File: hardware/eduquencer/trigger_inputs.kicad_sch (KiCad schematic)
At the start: 15 parts, among them Q1 MMBT3904

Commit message: Hardware: add test points, tiny cleanup
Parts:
- J?: value Jack_Trigger_In_B -> Reset In
- J?: value Jack_Trigger_In_A -> Clock In
- Q1, Q?: LCSC C20526 -> (none); LCSC Part # C20526 -> (none)
- R14, R15, R? (x2): LCSC C25803 -> (none); LCSC Part # C25803 -> (none)
- R16, R?: LCSC C4216 -> (none); LCSC Part # C4216 -> (none)
- R17, R?: LCSC C25804 -> (none); LCSC Part # C25804 -> (none)
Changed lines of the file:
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@@
       (effects (font (size 1.27 1.27)) (justify left) hide)
     )
-    (property "LCSC Part #" "C20526" (id 4) (at 132.08 60.96 0)
-      (effects (font (size 1.27 1.27)) hide)
-    )
-    (property "LCSC" "C20526" (id 5) (at 132.08 60.96 0)
-      (effects (font (size 1.27 1.27)) hide)
-    )
     (pin "1")
     (pin "2")
@@
       (effects (font (size 1.27 1.27)) hide)
     )
-    (property "LCSC Part #" "C25804" (id 4) (at 134.62 46.99 0)
-      (effects (font (size 1.27 1.27)) hide)
-    )
-    (property "LCSC" "C25804" (id 5) (at 134.62 46.99 0)
-      (effects (font (size 1.27 1.27)) hide)
-    )
     (pin "1")
     (pin "2")
@@
     )
     (property "Datasheet" "~" (id 3) (at 69.85 43.18 0)
-      (effects (font (size 1.27 1.27)) hide)
-    )
-    (property "LCSC Part #" "C25803" (id 4) (at 69.85 43.18 0)
-      (effects (font (size 1.27 1.27)) hide)
-    )
-    (property "LCSC" "C25803" (id 5) (at 69.85 43.18 0)
       (effects (font (size 1.27 1.27)) hide)
     )
@@
       (effects (font (size 1.27 1.27)) hide)
     )
-    (property "LCSC Part #" "C25803" (id 4) (at 96.52 60.96 0)
-      (effects (font (size 1.27 1.27)) hide)
-    )
-    (property "LCSC" "C25803" (id 5) (at 96.52 60.96 0)
-      (effects (font (size 1.27 1.27)) hide)
-    )
     (pin "1")
     (pin "2")
@@
     )
     (property "Datasheet" "~" (id 3) (at 118.11 74.93 0)
-      (effects (font (size 1.27 1.27)) hide)
-    )
-    (property "LCSC Part #" "C4216" (id 4) (at 118.11 74.93 0)
-      (effects (font (size 1.27 1.27)) hide)
-    )
-    (property "LCSC" "C4216" (id 5) (at 118.11 74.93 0)
       (effects (font (size 1.27 1.27)) hide)
     )
@@
   (symbol (lib_id "power:GND") (at 83.82 162.56 0) (unit 1)
     (in_bom yes) (on_board yes)
-    (property "Reference" "#PWR?" (id 0) (at 83.82 168.91 0)
+    (property "Reference" "#PWR0163" (id 0) (at 83.82 168.91 0)
       (effects (font (size 1.27 1.27)) hide)
     )
@@
   (symbol (lib_id "power:GND") (at 134.62 162.56 0) (unit 1)
     (in_bom yes) (on_board yes)
-    (property "Reference" "#PWR?" (id 0) (at 134.62 168.91 0)
+    (property "Reference" "#PWR0161" (id 0) (at 134.62 168.91 0)
       (effects (font (size 1.27 1.27)) hide)
     )
@@
   (symbol (lib_id "power:GND") (at 118.11 162.56 0) (unit 1)
     (in_bom yes) (on_board yes)
-    (property "Reference" "#PWR?" (id 0) (at 118.11 168.91 0)
+    (property "Reference" "#PWR0160" (id 0) (at 118.11 168.91 0)
       (effects (font (size 1.27 1.27)) hide)
     )
@@
       (effects (font (size 1.27 1.27)) hide)
     )
-    (property "LCSC Part #" "C25803" (id 4) (at 96.52 140.97 0)
-      (effects (font (size 1.27 1.27)) hide)
-    )
-    (property "LCSC" "C25803" (id 5) (at 96.52 140.97 0)
-      (effects (font (size 1.27 1.27)) hide)
-    )
     (pin "1")
     (pin "2")
@@
       (effects (font (size 1.27 1.27)) (justify right))
     )
-    (property "Value" "Jack_Trigger_In_B" (id 1) (at 50.8 141.6049 0)
+    (property "Value" "Reset In" (id 1) (at 50.8 141.6049 0)
       (effects (font (size 1.27 1.27)) (justify right))
     )
@@
       (effects (font (size 1.27 1.27)) (justify right))
     )
-    (property "Value" "Jack_Trigger_In_A" (id 1) (at 50.8 61.5949 0)
+    (property "Value" "Clock In" (id 1) (at 50.8 61.5949 0)
       (effects (font (size 1.27 1.27)) (justify right))
     )
@@
       (effects (font (size 1.27 1.27)) hide)
     )
-    (property "LCSC Part #" "C25803" (id 4) (at 69.85 123.19 0)
-      (effects (font (size 1.27 1.27)) hide)
-    )
-    (property "LCSC" "C25803" (id 5) (at 69.85 123.19 0)
-      (effects (font (size 1.27 1.27)) hide)
-    )
     (pin "1")
     (pin "2")
@@
   (symbol (lib_id "power:GND") (at 64.77 148.59 0) (unit 1)
     (in_bom yes) (on_board yes)
-    (property "Reference" "#PWR?" (id 0) (at 64.77 154.94 0)
+    (property "Reference" "#PWR0164" (id 0) (at 64.77 154.94 0)
       (effects (font (size 1.27 1.27)) hide)
     )
@@
       (effects (font (size 1.27 1.27)) (justify left) hide)
     )
-    (property "LCSC Part #" "C20526" (id 4) (at 132.08 140.97 0)
-      (effects (font (size 1.27 1.27)) hide)
-    )
-    (property "LCSC" "C20526" (id 5) (at 132.08 140.97 0)
-      (effects (font (size 1.27 1.27)) hide)
-    )
     (pin "1")
     (pin "2")
@@
   (symbol (lib_id "power:GND") (at 220.98 57.15 0) (unit 1)
     (in_bom yes) (on_board yes)
-    (property "Reference" "#PWR?" (id 0) (at 220.98 63.5 0)
+    (property "Reference" "#PWR0165" (id 0) (at 220.98 63.5 0)
       (effects (font (size 1.27 1.27)) hide)
     )
@@
     )
     (property "Datasheet" "~" (id 3) (at 134.62 127 0)
-      (effects (font (size 1.27 1.27)) hide)
-    )
-    (property "LCSC Part #" "C25804" (id 4) (at 134.62 127 0)
-      (effects (font (size 1.27 1.27)) hide)
-    )
-    (property "LCSC" "C25804" (id 5) (at 134.62 127 0)
       (effects (font (size 1.27 1.27)) hide)
     )
@@
       (effects (font (size 1.27 1.27)) hide)
     )
-    (property "LCSC Part #" "C4216" (id 4) (at 118.11 154.94 0)
-      (effects (font (size 1.27 1.27)) hide)
-    )
-    (property "LCSC" "C4216" (id 5) (at 118.11 154.94 0)
-      (effects (font (size 1.27 1.27)) hide)
-    )
     (pin "1")
     (pin "2")
@@
   (symbol (lib_id "power:+3.3V") (at 134.62 120.65 0) (unit 1)
     (in_bom yes) (on_board yes)
-    (property "Reference" "#PWR?" (id 0) (at 134.62 124.46 0)
+    (property "Reference" "#PWR0162" (id 0) (at 134.62 124.46 0)
       (effects (font (size 1.27 1.27)) hide)
     )
@@
   (symbol (lib_id "power:+3.3V") (at 220.98 41.91 0) (unit 1)
     (in_bom yes) (on_board yes)
-    (property "Reference" "#PWR?" (id 0) (at 220.98 45.72 0)
-      (effects (font (size 1.27 1.27)) hide)
-    )
+    (property "Reference" "#PWR0166" (id 0) (at 220.98 45.72 0)
+      (effects (font (size 1.27 1.27)) hide)
+    )

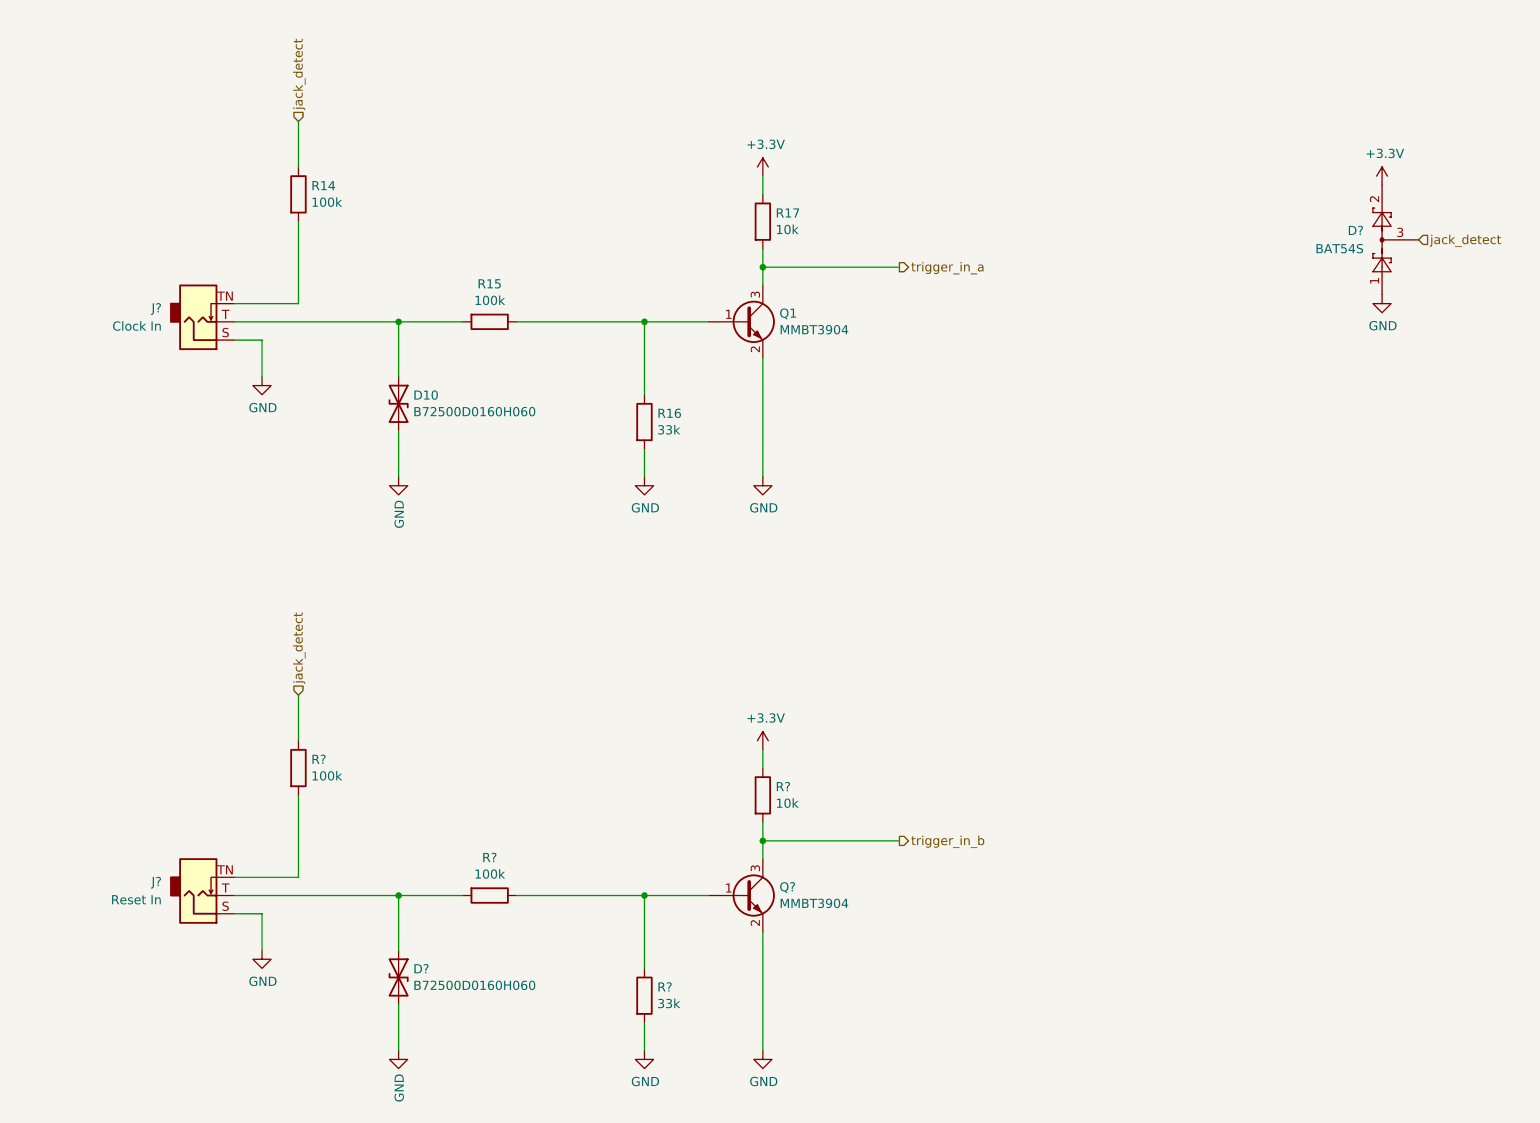
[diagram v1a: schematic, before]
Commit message: Hardware: update models, annotate, fix ERC issues
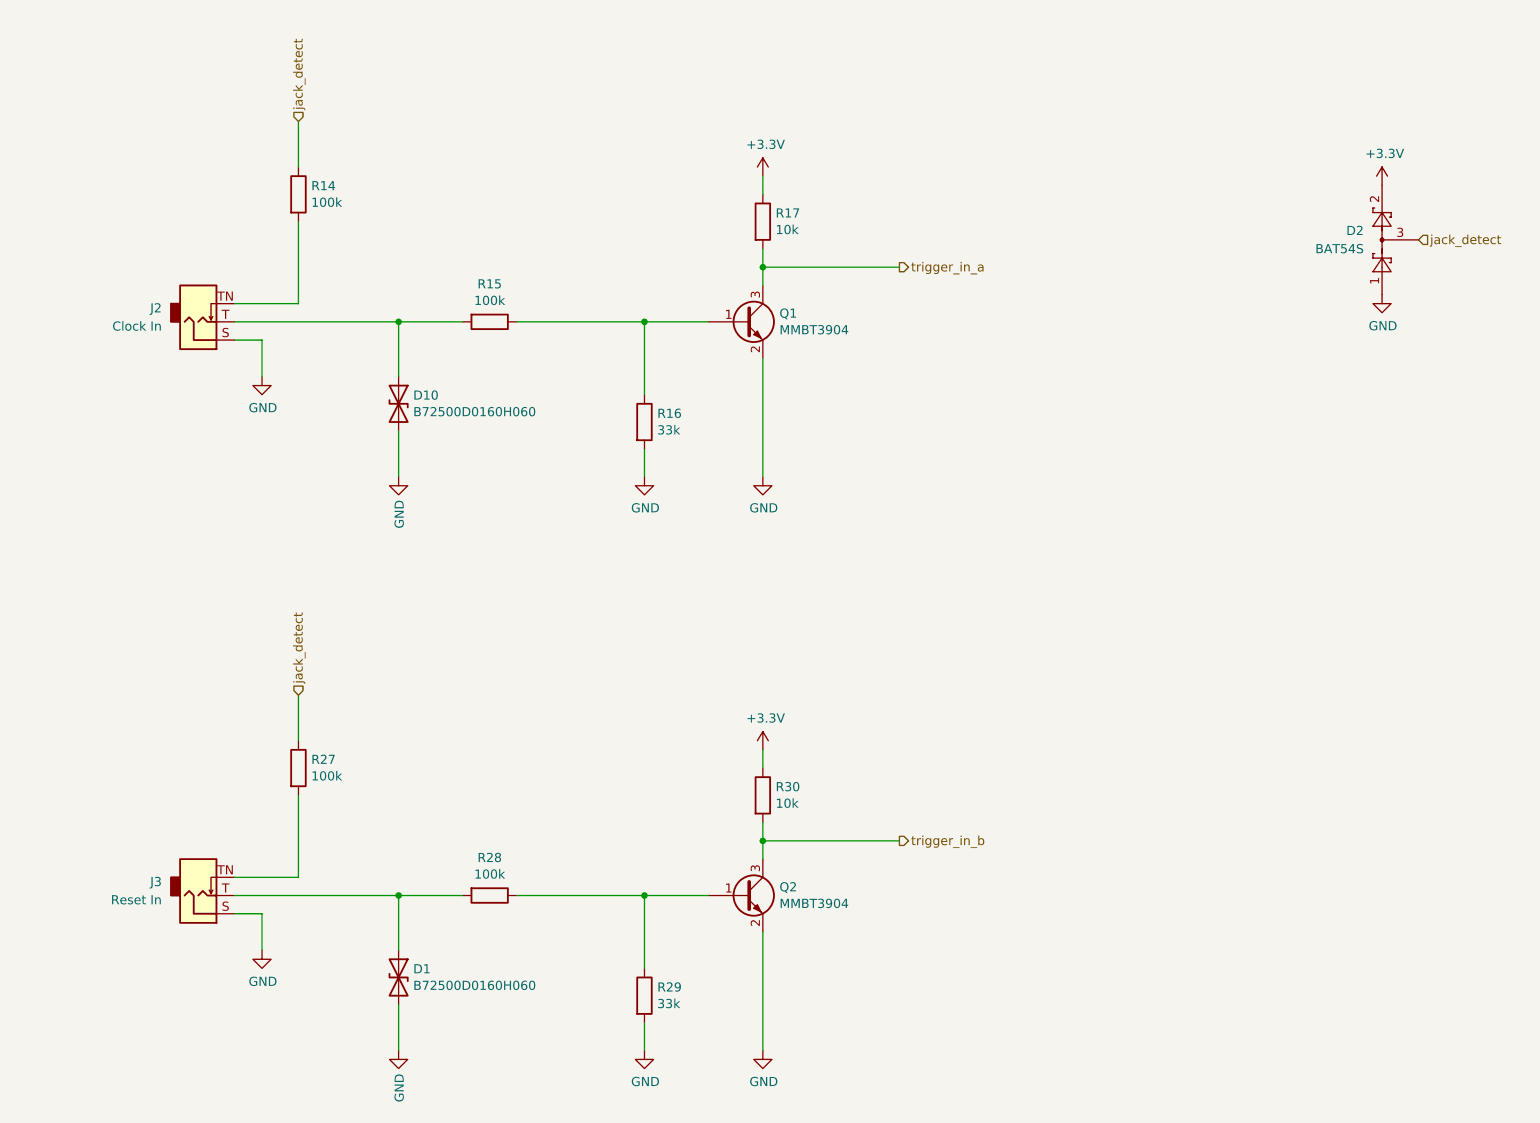
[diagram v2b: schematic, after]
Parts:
- gave numbers to parts that had none: 9
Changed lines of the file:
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@@
   (symbol (lib_id "Device:R") (at 96.52 140.97 270) (unit 1)
     (in_bom yes) (on_board yes)
-    (property "Reference" "R?" (id 0) (at 96.52 135.7122 90))
+    (property "Reference" "R28" (id 0) (at 96.52 135.7122 90))
     (property "Value" "100k" (id 1) (at 96.52 138.0236 90))
     (property "Footprint" "Resistor_SMD:R_0603_1608Metric" (id 2) (at 96.52 139.192 90)
@@
   (symbol (lib_id "Connector:AudioJack2_SwitchT") (at 55.88 140.97 0) (mirror x) (unit 1)
     (in_bom yes) (on_board yes) (fields_autoplaced)
-    (property "Reference" "J?" (id 0) (at 50.8 139.0649 0)
+    (property "Reference" "J3" (id 0) (at 50.8 139.0649 0)
       (effects (font (size 1.27 1.27)) (justify right))
     )
@@
   (symbol (lib_id "Connector:AudioJack2_SwitchT") (at 55.88 60.96 0) (mirror x) (unit 1)
     (in_bom yes) (on_board yes) (fields_autoplaced)
-    (property "Reference" "J?" (id 0) (at 50.8 59.0549 0)
+    (property "Reference" "J2" (id 0) (at 50.8 59.0549 0)
       (effects (font (size 1.27 1.27)) (justify right))
     )
@@
   (symbol (lib_id "Device:R") (at 69.85 123.19 0) (unit 1)
     (in_bom yes) (on_board yes)
-    (property "Reference" "R?" (id 0) (at 71.628 122.0216 0)
+    (property "Reference" "R27" (id 0) (at 71.628 122.0216 0)
       (effects (font (size 1.27 1.27)) (justify left))
     )
@@
   (symbol (lib_id "Transistor_BJT:MMBT3904") (at 132.08 140.97 0) (unit 1)
     (in_bom yes) (on_board yes)
-    (property "Reference" "Q?" (id 0) (at 136.9314 139.8016 0)
+    (property "Reference" "Q2" (id 0) (at 136.9314 139.8016 0)
       (effects (font (size 1.27 1.27)) (justify left))
     )
@@
   (symbol (lib_id "Device:R") (at 134.62 127 0) (unit 1)
     (in_bom yes) (on_board yes)
-    (property "Reference" "R?" (id 0) (at 136.398 125.8316 0)
+    (property "Reference" "R30" (id 0) (at 136.398 125.8316 0)
       (effects (font (size 1.27 1.27)) (justify left))
     )
@@
   (symbol (lib_id "Diode:BAT54S") (at 220.98 49.53 90) (unit 1)
     (in_bom yes) (on_board yes) (fields_autoplaced)
-    (property "Reference" "D?" (id 0) (at 218.44 48.2599 90)
+    (property "Reference" "D2" (id 0) (at 218.44 48.2599 90)
       (effects (font (size 1.27 1.27)) (justify left))
     )
@@
   (symbol (lib_id "Device:R") (at 118.11 154.94 0) (unit 1)
     (in_bom yes) (on_board yes)
-    (property "Reference" "R?" (id 0) (at 119.888 153.7716 0)
+    (property "Reference" "R29" (id 0) (at 119.888 153.7716 0)
       (effects (font (size 1.27 1.27)) (justify left))
     )
@@
   (symbol (lib_id "Device:D_TVS") (at 83.82 152.4 270) (unit 1)
     (in_bom yes) (on_board yes)
-    (property "Reference" "D?" (id 0) (at 85.852 151.2316 90)
+    (property "Reference" "D1" (id 0) (at 85.852 151.2316 90)
       (effects (font (size 1.27 1.27)) (justify left))
     )

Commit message: Hardware: assign all footprints
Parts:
- D1, D10: footprint Diode_SMD:D_0603_1608Metric -> Diode_SMD:D_0603_1608Metric_Pad1.05x0.95mm_HandSolder
- D2: footprint Package_TO_SOT_SMD:SOT-23 -> Package_TO_SOT_SMD:SOT-23_Handsoldering
- R14, R15, R16, R17, R27, R28, R29, R30: footprint Resistor_SMD:R_0603_1608Metric -> Resistor_SMD:R_0603_1608Metric_Pad0.98x0.95mm_HandSolder
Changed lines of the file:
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@@
       (effects (font (size 1.27 1.27)) (justify left))
     )
-    (property "Footprint" "Resistor_SMD:R_0603_1608Metric" (id 2) (at 132.842 46.99 90)
+    (property "Footprint" "Resistor_SMD:R_0603_1608Metric_Pad0.98x0.95mm_HandSolder" (id 2) (at 132.842 46.99 90)
       (effects (font (size 1.27 1.27)) hide)
     )
@@
       (effects (font (size 1.27 1.27)) (justify left))
     )
-    (property "Footprint" "Resistor_SMD:R_0603_1608Metric" (id 2) (at 68.072 43.18 90)
+    (property "Footprint" "Resistor_SMD:R_0603_1608Metric_Pad0.98x0.95mm_HandSolder" (id 2) (at 68.072 43.18 90)
       (effects (font (size 1.27 1.27)) hide)
     )
@@
     (property "Reference" "R15" (id 0) (at 96.52 55.7022 90))
     (property "Value" "100k" (id 1) (at 96.52 58.0136 90))
-    (property "Footprint" "Resistor_SMD:R_0603_1608Metric" (id 2) (at 96.52 59.182 90)
+    (property "Footprint" "Resistor_SMD:R_0603_1608Metric_Pad0.98x0.95mm_HandSolder" (id 2) (at 96.52 59.182 90)
       (effects (font (size 1.27 1.27)) hide)
     )
@@
       (effects (font (size 1.27 1.27)) (justify left))
     )
-    (property "Footprint" "Resistor_SMD:R_0603_1608Metric" (id 2) (at 116.332 74.93 90)
+    (property "Footprint" "Resistor_SMD:R_0603_1608Metric_Pad0.98x0.95mm_HandSolder" (id 2) (at 116.332 74.93 90)
       (effects (font (size 1.27 1.27)) hide)
     )
@@
       (effects (font (size 1.27 1.27)) (justify left))
     )
-    (property "Footprint" "Diode_SMD:D_0603_1608Metric" (id 2) (at 83.82 72.39 0)
+    (property "Footprint" "Diode_SMD:D_0603_1608Metric_Pad1.05x0.95mm_HandSolder" (id 2) (at 83.82 72.39 0)
       (effects (font (size 1.27 1.27)) hide)
     )
@@
     (property "Reference" "R28" (id 0) (at 96.52 135.7122 90))
     (property "Value" "100k" (id 1) (at 96.52 138.0236 90))
-    (property "Footprint" "Resistor_SMD:R_0603_1608Metric" (id 2) (at 96.52 139.192 90)
+    (property "Footprint" "Resistor_SMD:R_0603_1608Metric_Pad0.98x0.95mm_HandSolder" (id 2) (at 96.52 139.192 90)
       (effects (font (size 1.27 1.27)) hide)
     )
@@
       (effects (font (size 1.27 1.27)) (justify left))
     )
-    (property "Footprint" "Resistor_SMD:R_0603_1608Metric" (id 2) (at 68.072 123.19 90)
+    (property "Footprint" "Resistor_SMD:R_0603_1608Metric_Pad0.98x0.95mm_HandSolder" (id 2) (at 68.072 123.19 90)
       (effects (font (size 1.27 1.27)) hide)
     )
@@
       (effects (font (size 1.27 1.27)) (justify left))
     )
-    (property "Footprint" "Resistor_SMD:R_0603_1608Metric" (id 2) (at 132.842 127 90)
+    (property "Footprint" "Resistor_SMD:R_0603_1608Metric_Pad0.98x0.95mm_HandSolder" (id 2) (at 132.842 127 90)
       (effects (font (size 1.27 1.27)) hide)
     )
@@
       (effects (font (size 1.27 1.27)) (justify left))
     )
-    (property "Footprint" "Package_TO_SOT_SMD:SOT-23" (id 2) (at 217.805 47.625 0)
+    (property "Footprint" "Package_TO_SOT_SMD:SOT-23_Handsoldering" (id 2) (at 217.805 47.625 0)
       (effects (font (size 1.27 1.27)) (justify left) hide)
     )
@@
       (effects (font (size 1.27 1.27)) (justify left))
     )
-    (property "Footprint" "Resistor_SMD:R_0603_1608Metric" (id 2) (at 116.332 154.94 90)
+    (property "Footprint" "Resistor_SMD:R_0603_1608Metric_Pad0.98x0.95mm_HandSolder" (id 2) (at 116.332 154.94 90)
       (effects (font (size 1.27 1.27)) hide)
     )
@@
       (effects (font (size 1.27 1.27)) (justify left))
     )
-    (property "Footprint" "Diode_SMD:D_0603_1608Metric" (id 2) (at 83.82 152.4 0)
-      (effects (font (size 1.27 1.27)) hide)
-    )
+    (property "Footprint" "Diode_SMD:D_0603_1608Metric_Pad1.05x0.95mm_HandSolder" (id 2) (at 83.82 152.4 0)
+      (effects (font (size 1.27 1.27)) hide)
+    )
